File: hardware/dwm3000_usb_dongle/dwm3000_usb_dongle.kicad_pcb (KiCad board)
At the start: 2 copper layers, 355 x 140 mm, 22 parts, among them J1 USB-4AM103AS, J2 3221-10-0300-00, U1 STM32C071F8P6, U2 XC6220B331MR-G

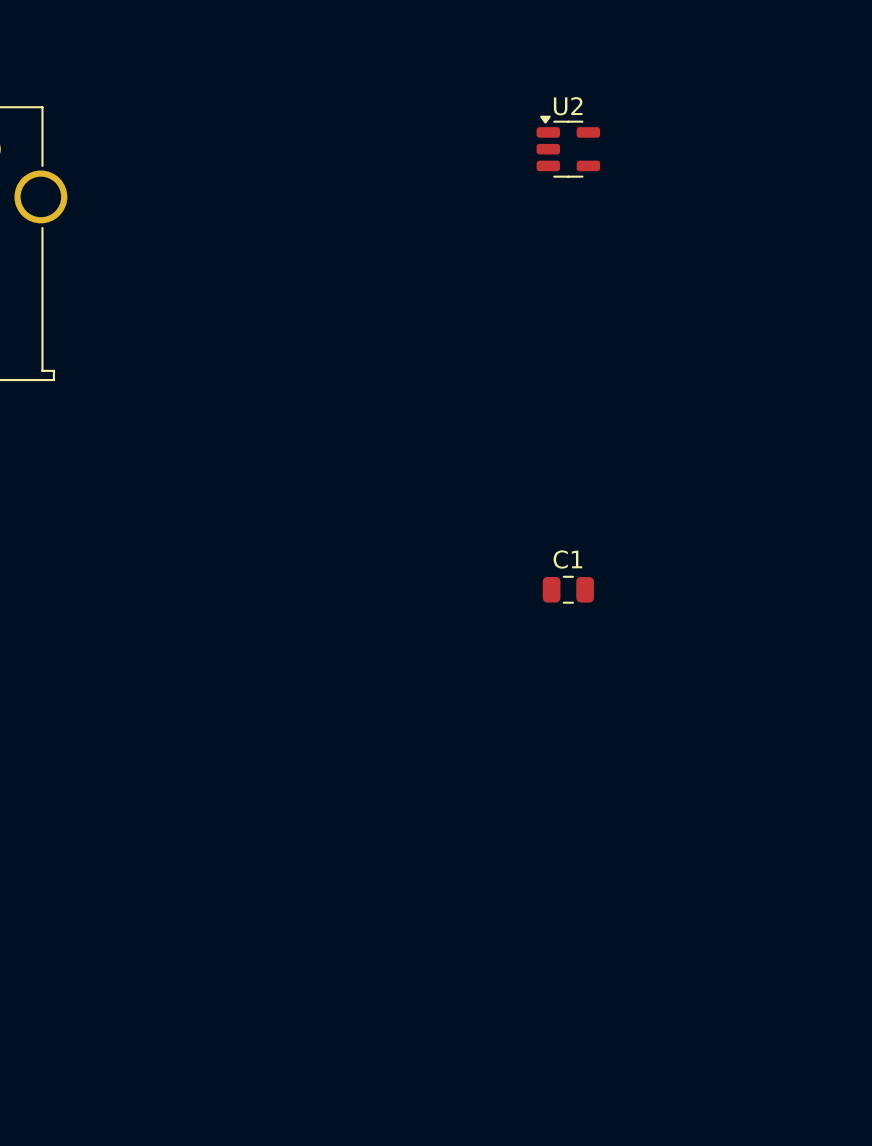
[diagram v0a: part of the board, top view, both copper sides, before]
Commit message: Add USB ESD protection, VBUS fuse/filtering, and power-indicator LED
Cross-checked against an independently-drawn reference schematic and
added the three subsystems it had that this project didn't:

- U3 (USBLC6-2SC6): dual-line USB D+/D- ESD protection, in series
  between the connector and the existing R1/R2 series resistors.
- F1 (500mA PTC fuse) + C4/C8 (100nF HF bypass caps): VBUS now passes
  through a fuse before becoming the board's +5V rail, with extra HF
  bypass at the connector and at the LDO input alongside the existing
  bulk caps.
- D5/R9: an always-on power-indicator LED across +3V3/GND, independent
  of the MCU (unlike the existing D1/D4 status LEDs).

All new chip R/C/LED parts use 0603 (1608 metric) footprints, matching
the rest of the design.

Fixed a bug found along the way: wire_to_power() was called with
"VBUS_RAW" as if it were a power-symbol net (like GND/+3V3/+5V), but
it's just a plain net label -- this referenced a nonexistent
power:VBUS_RAW symbol and crashed kicad-cli's parser. Also fixed U3's
pin routing: its 4 signal pins are only 2.54mm apart, so straight
same-length stubs produced overlapping labels; added a small
jog_label() helper to route each pin out with a short vertical jog
before the label.
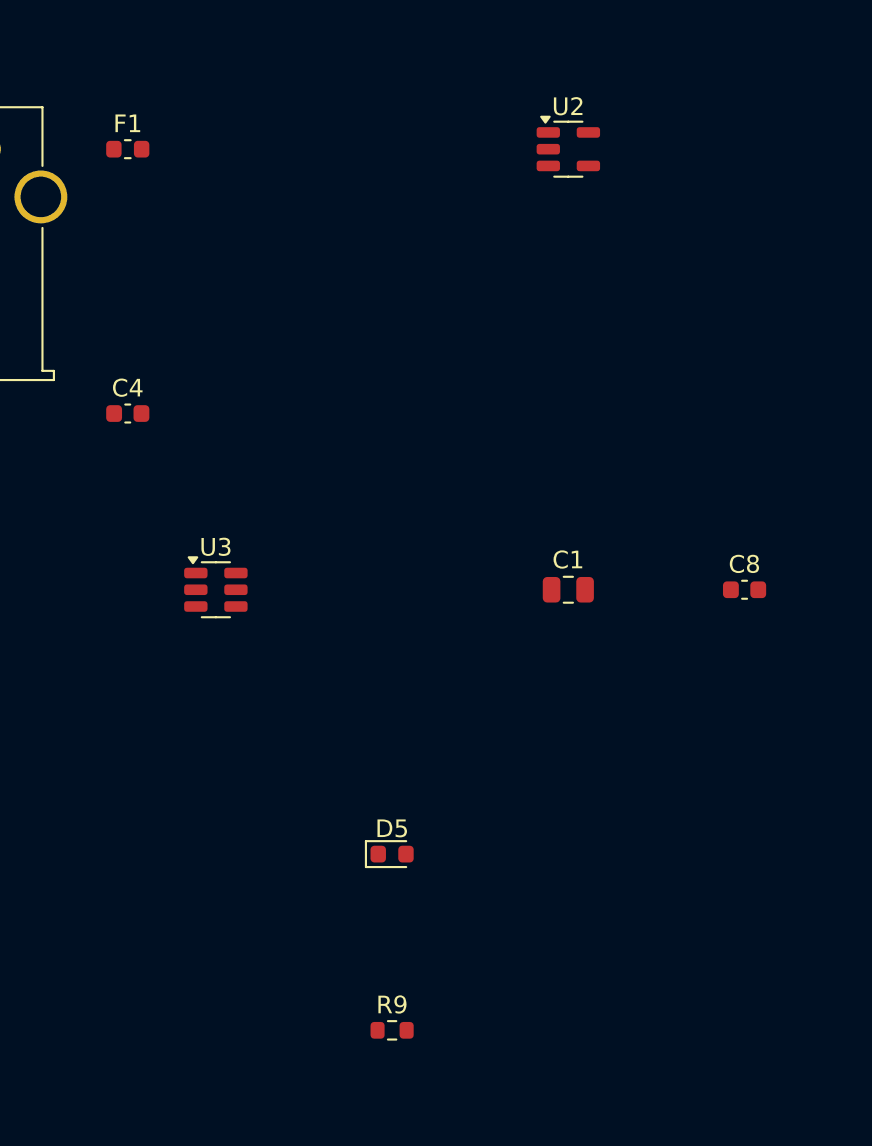
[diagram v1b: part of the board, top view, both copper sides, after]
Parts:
- added C4: 100nF, C_0603_1608Metric, F.Cu at (40.0, 45.0)
- added C8: 100nF, C_0603_1608Metric, F.Cu at (75.0, 55.0)
- added D5: LED, LED_0603_1608Metric, F.Cu at (55.0, 70.0)
- added F1: 500mA, Fuse_0603_1608Metric, F.Cu at (40.0, 30.0)
- added R9: 1k, R_0603_1608Metric, F.Cu at (55.0, 80.0)
- added U3: USBLC6-2SC6, SOT-23-6, F.Cu at (45.0, 55.0)
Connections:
- J1 pad 1: +5V -> /VBUS_RAW
- J1 pad 2: /USB_DM -> /USB_DM_RAW
- J1 pad 3: /USB_DP -> /USB_DP_RAW
